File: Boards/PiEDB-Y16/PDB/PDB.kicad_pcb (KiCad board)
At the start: 2 copper layers, 112.1 x 88.3 mm, 56 parts, among them J1 Conn_01x02, J2 Conn_01x04, Q1 s8050_JSMSEMI, SW2 SW_SPDT, Sw1 D-SWITCH_MR5-111-C5N-BB, U2 CH340G, U3 PCF8574, Y1 12MHz

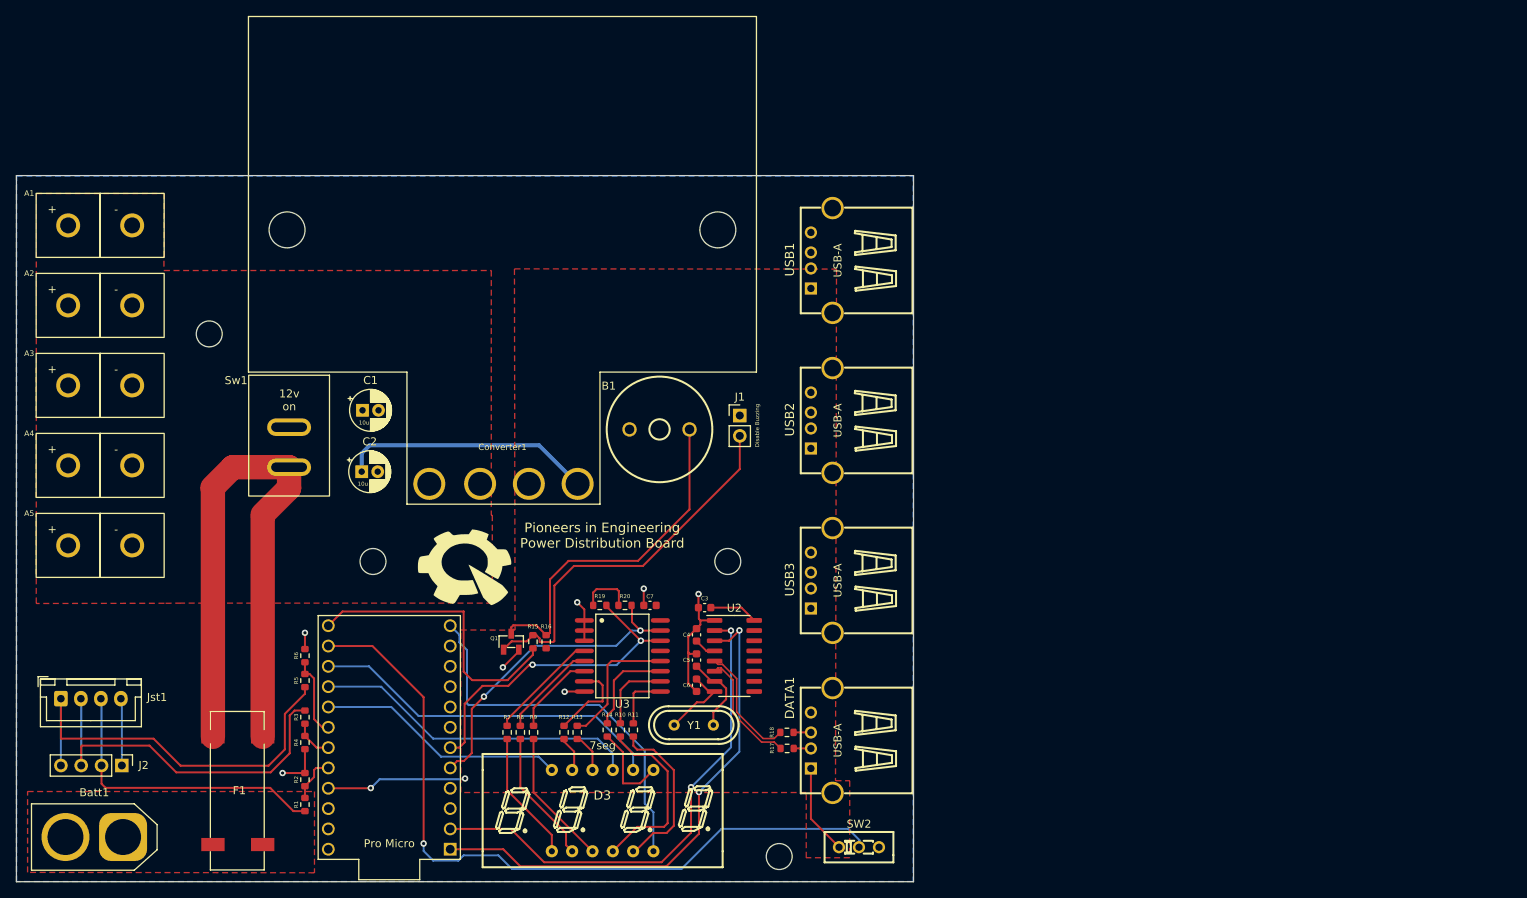
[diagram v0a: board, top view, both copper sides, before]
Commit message: finished servo layout
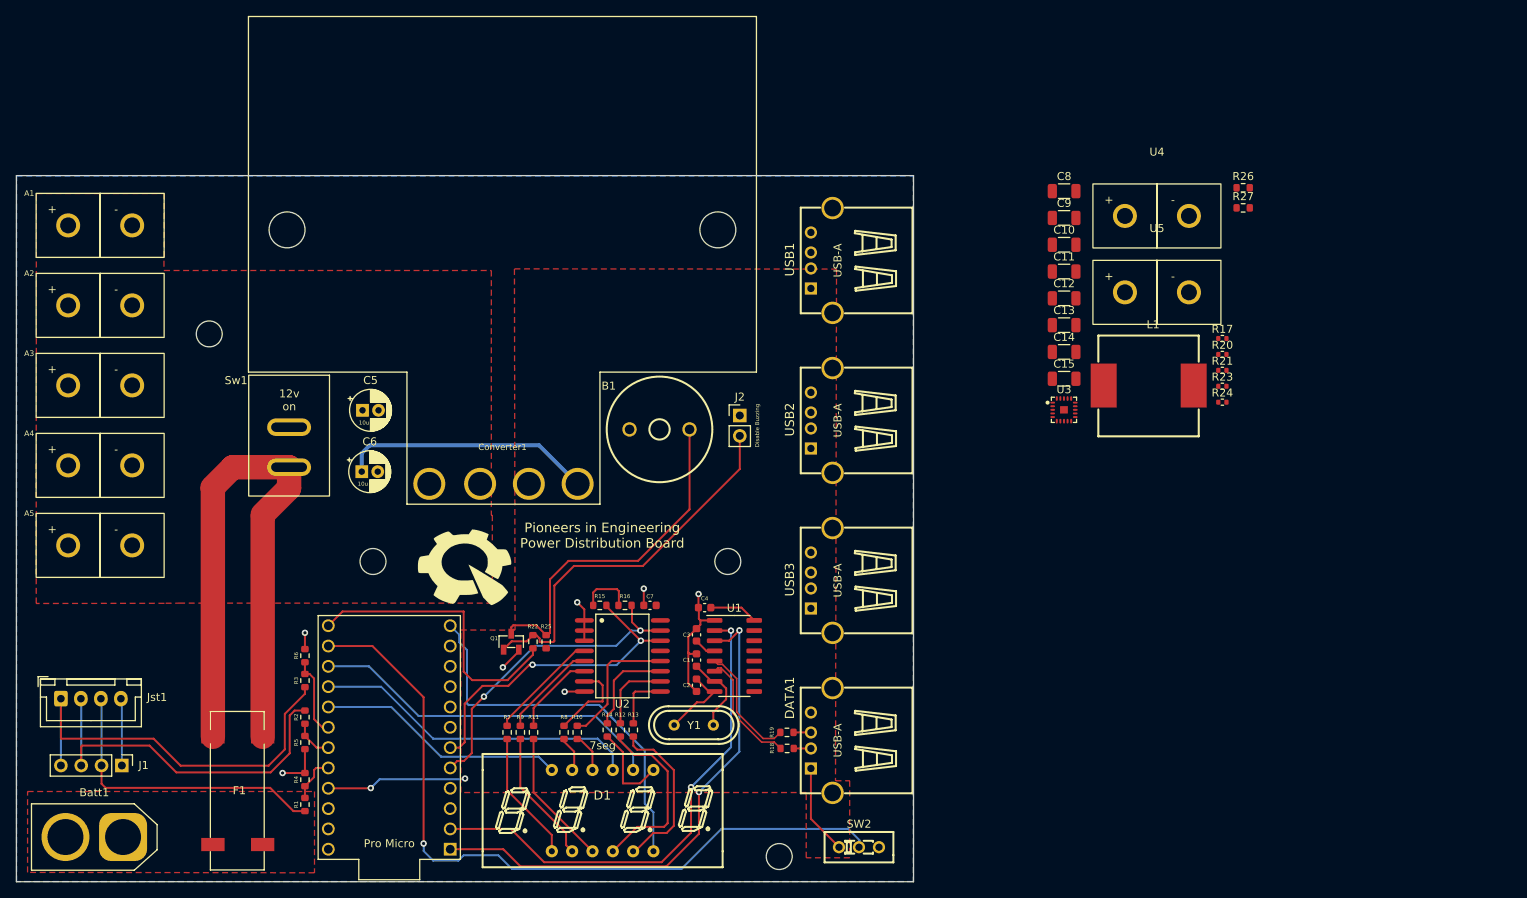
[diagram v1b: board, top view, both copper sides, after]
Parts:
- added C10: 0.1u, Capacitor_SMD:C_1206_3216Metric, F.Cu at (188.5, 25.5)
- added C11: 0.1u, Capacitor_SMD:C_1206_3216Metric, F.Cu at (188.5, 28.9)
- added C12: 47u, Capacitor_SMD:C_1206_3216Metric, F.Cu at (188.5, 32.2)
- added C13: 47u, Capacitor_SMD:C_1206_3216Metric, F.Cu at (188.5, 35.6)
- added C14: 47u, Capacitor_SMD:C_1206_3216Metric, F.Cu at (188.5, 38.9)
- added C15: 47u, Capacitor_SMD:C_1206_3216Metric, F.Cu at (188.5, 42.3)
- added C8: 22u, Capacitor_SMD:C_1206_3216Metric, F.Cu at (188.5, 18.8)
- added C9: 22u, Capacitor_SMD:C_1206_3216Metric, F.Cu at (188.5, 22.2)
- added L1: 1.8u, PiE_Footprints:125CDMCCDS-1R8MC, F.Cu at (199.6, 43.1)
- added R17: 100k, Resistor_SMD:R_0402_1005Metric, F.Cu at (208.3, 37.3)
- added R20: 100k, Resistor_SMD:R_0402_1005Metric, F.Cu at (208.3, 39.2)
- added R21: 51k, Resistor_SMD:R_0402_1005Metric, F.Cu at (208.3, 41.2)
- added R23: 200k, Resistor_SMD:R_0402_1005Metric, F.Cu at (208.3, 43.2)
- added R24: 33k, Resistor_SMD:R_0402_1005Metric, F.Cu at (208.3, 45.2)
- added R26: 110k, Resistor_SMD:R_0603_1608Metric, F.Cu at (210.9, 18.4)
- added R27: 15k, Resistor_SMD:R_0603_1608Metric, F.Cu at (210.9, 20.9)
- added U3: ~, PiE_Footprints:TPS56C230RJER, F.Cu at (188.5, 46.2)
- added U4: Anderson_Horizontal, PiE_Footprints:anderson_horizontal, F.Cu at (200.1, 17.9)
- added U5: Anderson_Horizontal, PiE_Footprints:anderson_horizontal, F.Cu at (200.1, 27.5)
- Converter1: value BUCK_CONVERTER_5V -> 5v_converter
- renumbered C5 to C1, C6 to C2, C4 to C3, C3 to C4, C1 to C5, C2 to C6, D3 to D1, J2 to J1, J1 to J2, R13 to R10, R9 to R11, R10 to R12, R11 to R13, R19 to R15, R20 to R16, R17 to R18, R18 to R19, R3 to R2, R15 to R22, R16 to R25, R5 to R3, R2 to R4, R4 to R5, R12 to R8, R8 to R9, U2 to U1, U3 to U2
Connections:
- Jst1 pad 4: GND -> unconnected-(Jst1-GND-Pad4)

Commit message: Worked on PDB Revision
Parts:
- removed Converter1: 5v_converter, PiE_Footprints:5v_converter
- removed U4, U5: Anderson_Horizontal, PiE_Footprints:anderson_horizontal
- added C16: 1u, Capacitor_SMD:C_0805_2012Metric, F.Cu at (188.7, 49.7)
- R21: value 51k -> 15k
- moved C11 39.7 mm to (227.9, 33.8), turned to 180 degrees
- moved L1 38.2 mm to (237.7, 39.8)
- moved U3 37.6 mm to (225.6, 40.2), turned to -90 degrees
- moved C8 35.3 mm to (220.4, 33.8)
- moved C9 34.9 mm to (220.4, 36.3)
- moved C10 34.6 mm to (220.4, 38.8)
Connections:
- C10 pad 2: /Vin -> /12v
- C12 pad 2: /Vout -> /5v
- C13 pad 2: /Vout -> /5v
- C14 pad 2: /Vout -> /5v
- C15 pad 2: /Vout -> /5v
- C8 pad 2: /Vin -> /12v
- C9 pad 2: /Vin -> /12v
- L1 pad 2: /Vout -> /5v
- R20 pad 1: /VCC -> /12v
- U3 pad 2: /Vin -> /12v
- U3 pad 3: /Vin -> /12v
- U3 pad 4: /Vin -> /12v
- U3 pad 5: /Vin -> /12v
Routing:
- net /fuse out: track 76.9 -> 0.00 mm
- net /BST: track 0.00 -> 5.03 mm
- net GND: track 45.2 -> 46.2 mm, vias 7 -> 10
- added copper zone on F.Cu, net /SW
- added copper zone on F.Cu, net /fuse out

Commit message: pictures of layout
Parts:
- moved R26 30.5 mm to (224.5, 45.7), turned to 90 degrees
- moved R27 26.7 mm to (225.3, 43.4)
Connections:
- R26 pad 1: /Vout -> /5v
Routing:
- net /FB: track 0.00 -> 4.33 mm

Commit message: Revision of PDB
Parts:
- added J3: Conn_01x02, PiE_Footprints:PinHeader_1x02_P2.54mm_Vertical, F.Cu at (150.0, 92.5)
- added R28: 10k, Resistor_SMD:R_0402_1005Metric, F.Cu at (103.8, 36.6)
- added SW3: SW_MEC_5E, Button_Switch_THT:SW_PUSH_6mm, F.Cu at (82.3, 20.5)
- moved C8 120.9 mm to (99.5, 29.8), turned to 90 degrees
- moved C9 118.6 mm to (102.0, 29.8), turned to 90 degrees
- moved C10 116.2 mm to (104.5, 29.8), turned to 90 degrees
- moved R26 113.4 mm to (111.6, 36.0)
- moved R27 113.4 mm to (112.3, 33.8)
- moved U3 112.4 mm to (113.7, 29.6)
- moved C11 112.4 mm to (116.0, 23.2)
- moved L1 108.7 mm to (129.5, 28.4)
- moved R20 100.0 mm to (108.6, 31.4), turned to -90 degrees
- moved R21 99.5 mm to (109.1, 33.1)
- moved R17 97.8 mm to (110.8, 30.1)
- moved R24 94.3 mm to (114.6, 34.0), turned to -90 degrees
- moved R23 93.8 mm to (115.1, 32.4), turned to 180 degrees
- moved C16 75.1 mm to (114.6, 37.0), turned to -90 degrees
- moved C12 51.9 mm to (136.7, 35.1), turned to 90 degrees
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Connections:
- DATA1 pad 1: /5v -> Net-(DATA1-VCC)
- Pro1 pad 8: unconnected-(Pro1-5-Pad8) -> /BatCal
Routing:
- net /5v: track 73.6 -> 177.7 mm, vias 2 -> 4
- net /BatCal: track 0.00 -> 76.2 mm, vias 0 -> 3
- net /VCC: track 0.00 -> 20.0 mm, vias 0 -> 2
- net GND: track 46.2 -> 39.4 mm, vias 10 -> 84
- net /EN: track 0.00 -> 6.53 mm
- net /12v: track 0.00 -> 6.31 mm
- net Net-(DATA1-VCC): track 0.00 -> 4.45 mm
- net /SW: track 0.00 -> 2.88 mm
- net /MODE: track 0.00 -> 2.51 mm
- net /FB: track 4.33 -> 6.63 mm
- net /BST: track 5.03 -> 6.82 mm
- net Net-(U3-PGOOD): track 0.00 -> 1.05 mm
- net /D+: track 15.0 -> 14.2 mm
- net Net-(DATA1-D-): track 2.15 -> 2.90 mm
- net /D-: track 15.0 -> 14.3 mm
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- added copper zone on F.Cu, net GND
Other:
- board size 112.1 x 88.3 mm -> 112.1 x 88.2 mm
- board text added: "Copyright (c) 2024, Pioneers in Engineering All rights reserved. Design by: Justin H This design is open source hardware. For more information, visit github.com/pioneers/PiElectrical"
- board text removed: "12v"
- board text removed: "5v"
- board text removed: "Copyright (c) 2023, Pioneers in Engineering All rights reserved. Design by: Justin H With help from: Ricky L This design is open source hardware. For more information, visit github.com/pioneers/PiElectrical"

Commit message: made new PDB prototype
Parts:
- added C17: 1u, Capacitor_SMD:C_0402_1005Metric, F.Cu at (111.0, 36.1)
- C11: footprint Capacitor_SMD:C_1206_3216Metric -> Capacitor_SMD:C_0402_1005Metric
- C16: footprint Capacitor_SMD:C_0805_2012Metric -> Capacitor_SMD:C_0402_1005Metric
- R22: value 3300 -> 2000
- R25: value 1000 -> 100
- R26, R27: footprint Resistor_SMD:R_0603_1608Metric -> Resistor_SMD:R_0402_1005Metric
- moved SW3 53.7 mm to (61.3, 70.0)
- moved R28 50.9 mm to (70.0, 74.8), turned to -90 degrees
- moved C8 12.6 mm to (109.3, 22.0), turned to 0 degrees
- moved C9 9.06 mm to (109.3, 24.5), turned to 0 degrees
- moved R25 7.61 mm to (116.2, 73.9)
- moved C11 7.29 mm to (117.7, 30.3), turned to 90 degrees
- moved R22 6.53 mm to (116.2, 77.8)
- moved C10 5.59 mm to (109.3, 27.0), turned to 0 degrees
- moved R21 4.52 mm to (108.2, 28.7), turned to 180 degrees
- moved L1 3.86 mm to (130.8, 24.8)
- moved R20 3.43 mm to (110.7, 28.7), turned to 180 degrees
- moved R26 3.13 mm to (114.5, 37.1)
- moved R27 2.92 mm to (113.0, 36.6), turned to 180 degrees
- moved C16 2.66 mm to (117.2, 37.9)
- moved U3 2.47 mm to (114.0, 32.0)
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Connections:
- J2 pad 2: /base -> /Buzzer
- Q1 pad 1: /base -> Net-(Q1-B)
- R22 pad 1: /Buzzer -> GND
- R22 pad 2: /base -> Net-(Q1-B)
- R25 pad 1: /5v -> Net-(Q1-B)
- R25 pad 2: /collector -> /Buzzer
- U3 pad 11: unconnected-(U3-SS-Pad11) -> Net-(U3-SS)
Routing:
- net /base: track 48.1 -> 0.00 mm
- net GND: track 39.4 -> 78.8 mm, vias 84 -> 87
- net /Buzzer: track 36.4 -> 68.8 mm
- net /5v: track 177.7 -> 163.6 mm, vias 4 -> 5
- net /BatCal: track 76.2 -> 64.0 mm, vias 3 -> 2
- net /collector: track 43.9 -> 34.8 mm
- net /12v: track 6.31 -> 0.00 mm
- net Net-(Q1-B): track 0.00 -> 5.06 mm
- net /SW: track 2.88 -> 7.90 mm, vias 0 -> 2
- net /EN: track 6.53 -> 11.0 mm, vias 0 -> 2
- net /BST: track 6.82 -> 3.17 mm
- net Net-(U3-SS): track 0.00 -> 3.38 mm
- net /FB: track 6.63 -> 4.18 mm
- net /VCC: track 20.0 -> 18.1 mm

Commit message: PDB Updates
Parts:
- U1: footprint PiE_Footprints:CH340g -> Package_SO:SOP-16_3.9x9.9mm_P1.27mm
